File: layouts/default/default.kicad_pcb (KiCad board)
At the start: 2 copper layers, 120 x 130 mm, 83 parts

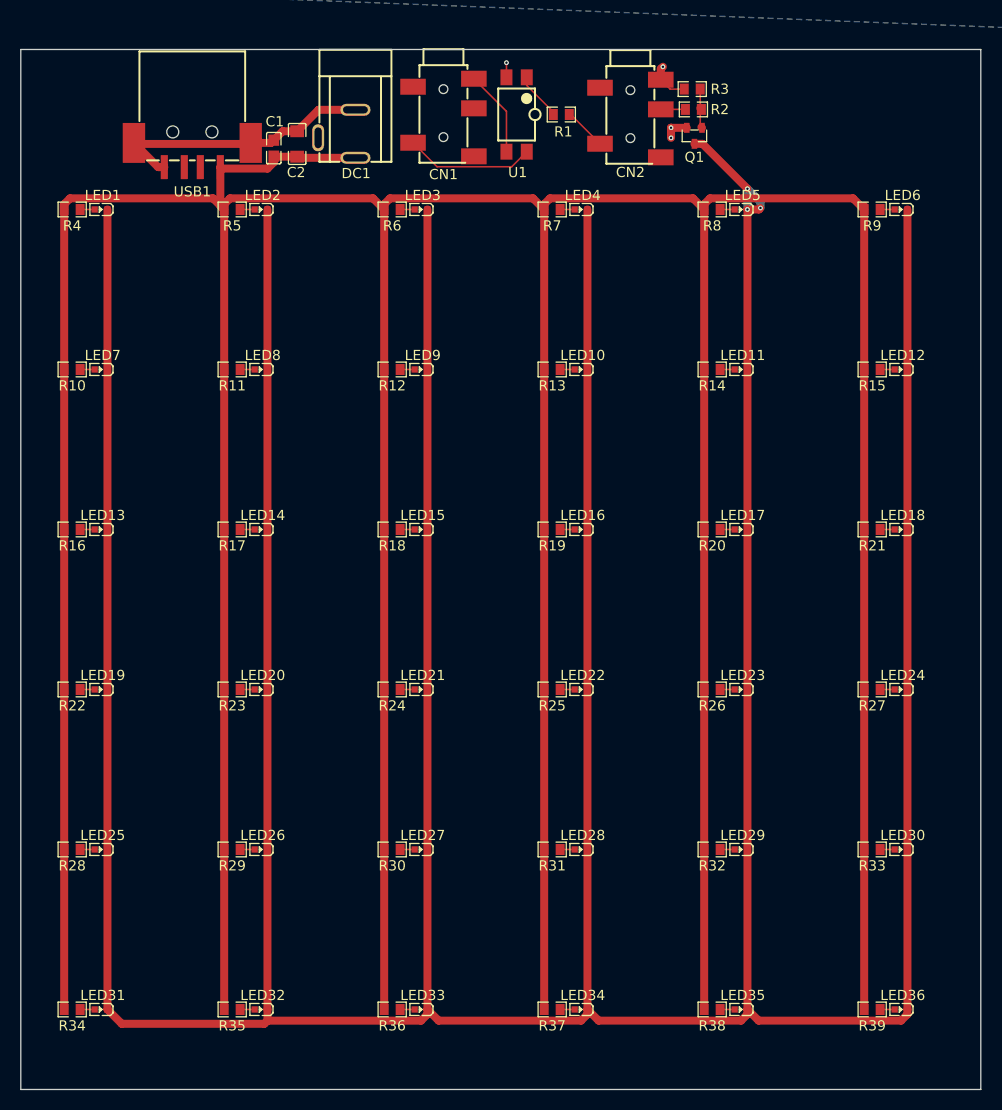
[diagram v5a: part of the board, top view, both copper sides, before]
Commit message: just manually do mounting holes since the people at atopile are LYING to me
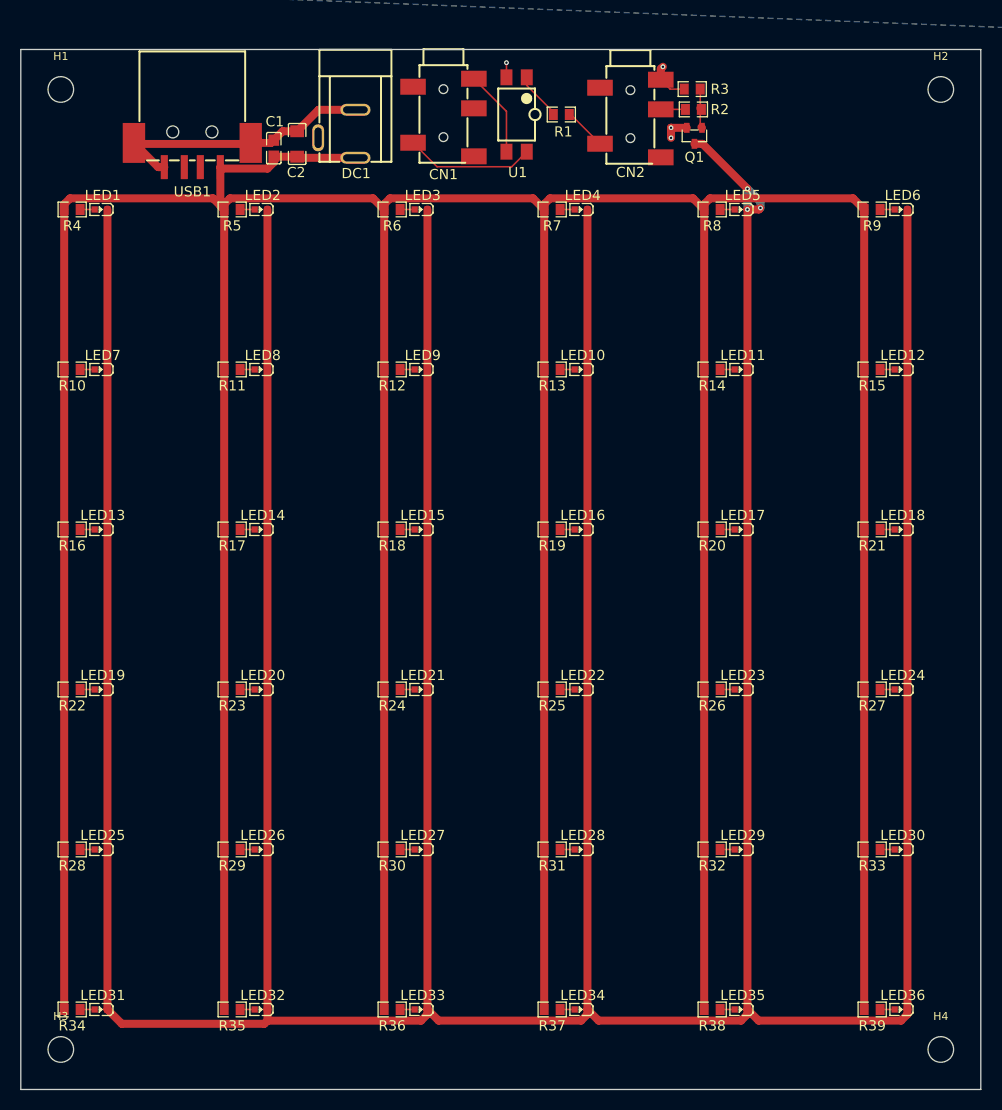
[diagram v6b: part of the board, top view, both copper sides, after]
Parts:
- added H1: MountingHole_3.2mm_M3, MountingHole:MountingHole_3.2mm_M3, F.Cu at (5.00, 5.00)
- added H2: MountingHole_3.2mm_M3, MountingHole:MountingHole_3.2mm_M3, F.Cu at (115.0, 5.00)
- added H3: MountingHole_3.2mm_M3, MountingHole:MountingHole_3.2mm_M3, F.Cu at (5.00, 125.0)
- added H4: MountingHole_3.2mm_M3, MountingHole:MountingHole_3.2mm_M3, F.Cu at (115.0, 125.0)

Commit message: done
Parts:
- H1, H2, H3, H4: value MountingHole_3.2mm_M3 -> (none)
